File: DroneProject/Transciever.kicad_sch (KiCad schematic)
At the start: 10 parts

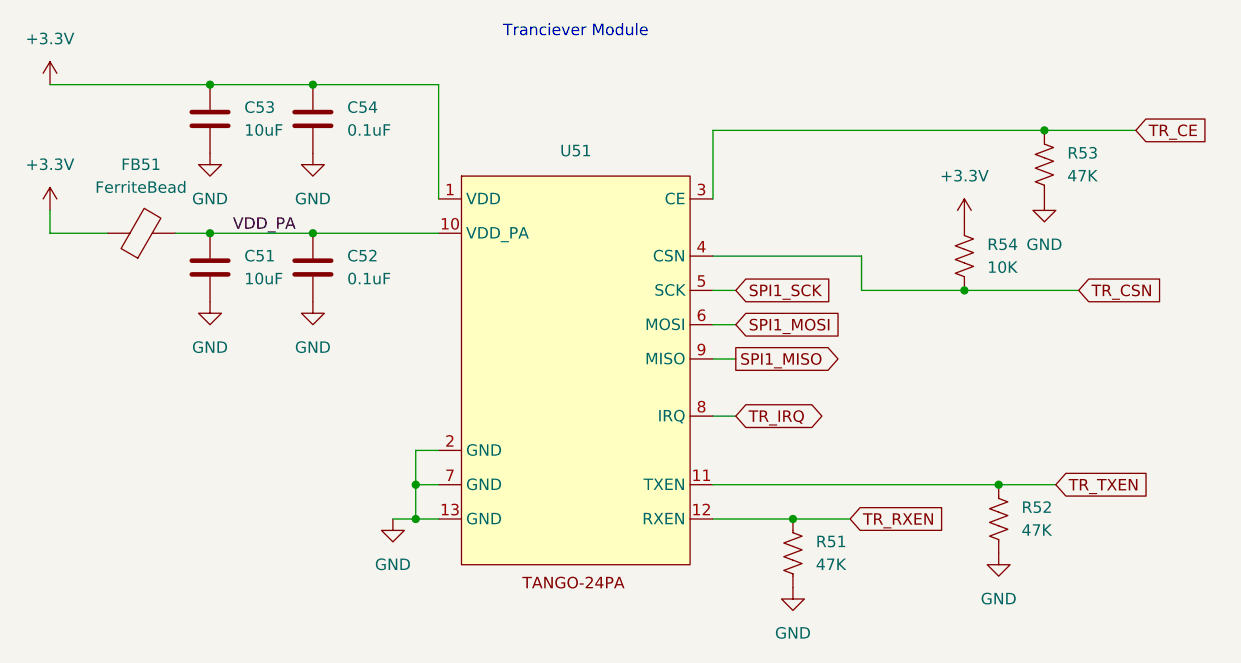
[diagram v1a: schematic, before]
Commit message: Changed motor controller to higher pin count MCU.  Defined all the pins for 3x PWM control over 4 motors.  Renamed a couple of global IO signals to indicate MCU origin (C0 vs C1)
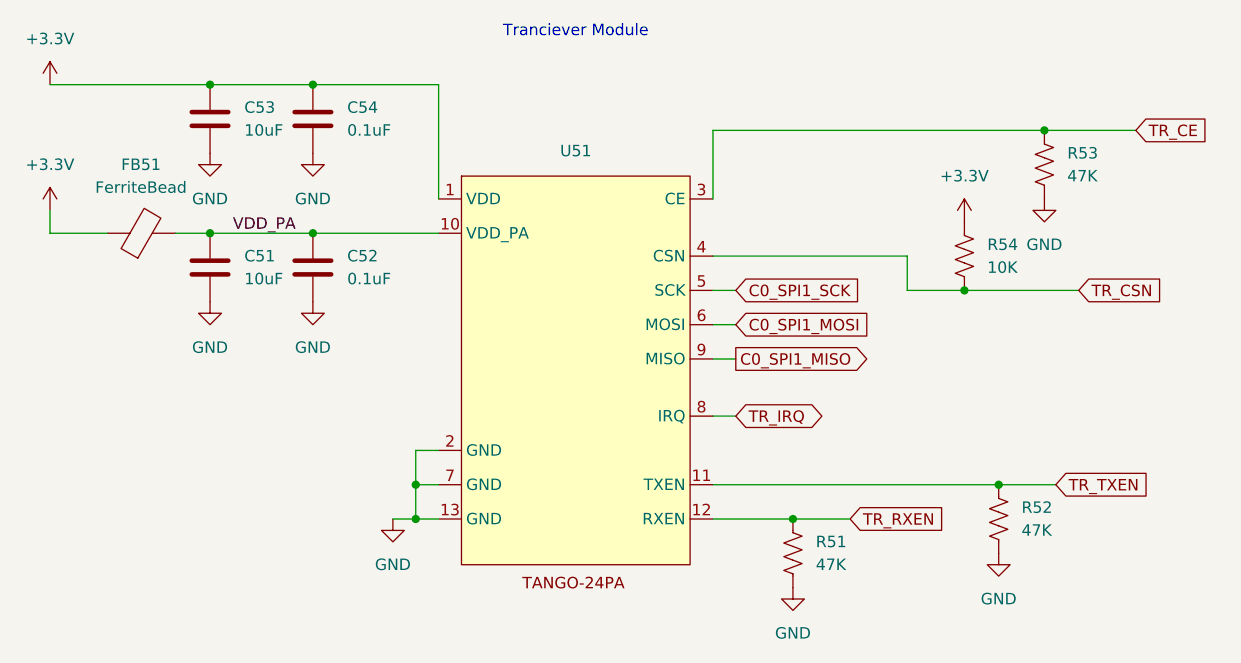
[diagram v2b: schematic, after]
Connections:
- net SPI1_MISO renamed C0_SPI1_MISO
- net SPI1_MOSI renamed C0_SPI1_MOSI
- net SPI1_SCK renamed C0_SPI1_SCK
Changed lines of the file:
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@@
 	(wire
 		(pts
-			(xy 176.53 83.82) (xy 160.02 83.82)
+			(xy 181.61 83.82) (xy 160.02 83.82)
 		)
 		(stroke
@@
 	(wire
 		(pts
-			(xy 176.53 87.63) (xy 187.96 87.63)
+			(xy 181.61 87.63) (xy 187.96 87.63)
 		)
 		(stroke
@@
 	(wire
 		(pts
-			(xy 176.53 87.63) (xy 176.53 83.82)
+			(xy 181.61 87.63) (xy 181.61 83.82)
 		)
 		(stroke
@@
 		)
 	)
-	(global_label "SPI1_MOSI"
+	(global_label "C0_SPI1_MOSI"
 		(shape input)
 		(at 162.56 91.44 0)
@@
 		)
 		(property "Intersheetrefs" "${INTERSHEET_REFS}"
-			(at 174.1933 91.44 0)
+			(at 178.8499 91.44 0)
 			(effects
 				(font
@@
 		)
 	)
-	(global_label "SPI1_MISO"
+	(global_label "C0_SPI1_MISO"
 		(shape output)
 		(at 162.56 95.25 0)
@@
 		)
 		(property "Intersheetrefs" "${INTERSHEET_REFS}"
-			(at 174.1933 95.25 0)
+			(at 178.8499 95.25 0)
 			(effects
 				(font
@@
 		)
 	)
-	(global_label "SPI1_SCK"
+	(global_label "C0_SPI1_SCK"
 		(shape input)
 		(at 162.56 87.63 0)
@@
 		)
 		(property "Intersheetrefs" "${INTERSHEET_REFS}"
-			(at 173.3466 87.63 0)
-			(effects
-				(font
+			(at 178.0032 87.63 0)
+			(effects
+				(font
